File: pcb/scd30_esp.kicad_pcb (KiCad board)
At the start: 2 copper layers, 59.2 x 39.4 mm, 60 parts, among them J1 SCD30, J2 USB_C_Receptacle_USB2.0, J3 24P P0.5mm waveshare E-paper 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, J4 QWIIC, Q1 Si1308EDL, Q2 Q_NMOS_GSD, Q3 BSS138PS, Q4 Q_NMOS_GSD, SW1 SW_SPST, U1 TPS62A01PDDCR, U2 ESP32-WROOM-E, U3 CH340C, U4 TSOP38G36

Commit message: RC1
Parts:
- added D7: LED_Small, LED_SMD:LED_0603_1608Metric, B.Cu at (112.6, 79.7)
- added R17: 1k, Resistor_SMD:R_0603_1608Metric, B.Cu at (115.8, 79.7)
- moved R13 13.2 mm to (142.3, 80.8), turned to 180 degrees
- moved R12 11.7 mm to (145.3, 80.8), turned to 0 degrees
- moved Q2 3.22 mm to (156.4, 83.1), turned to 0 degrees
- moved R14 2.97 mm to (117.1, 105.6)
- moved Q4 2.97 mm to (117.0, 110.0)
- moved R15 2.97 mm to (117.1, 107.2)
- moved R11 2.94 mm to (160.7, 82.5)
- moved R16 2.73 mm to (117.0, 114.3), turned to 90 degrees
- moved C7 2.42 mm to (113.5, 109.2)
- moved C6 2.33 mm to (161.9, 85.4), turned to -90 degrees
- moved SW1 1.00 mm to (158.0, 114.7)
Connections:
- U2 pad 24: unconnected-(U2-ADC2_CH2/GPIO2-Pad24) -> /status_led
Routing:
- net +3V3: track 187.3 -> 204.3 mm
- net /status_led: track 0.00 -> 15.4 mm, vias 0 -> 1
- net Net-(Q2-G): track 2.08 -> 9.86 mm
- net Net-(D6-K): track 2.52 -> 8.22 mm
- net VBUS: track 46.4 -> 42.6 mm
- net /IR_TX_L: track 51.2 -> 48.0 mm
- net GND: track 102.8 -> 99.8 mm
- net Net-(D5-K): track 2.58 -> 5.56 mm
- net /QWIIC_SDA: track 61.0 -> 59.1 mm
- net /QWIIC_SCL: track 62.5 -> 60.8 mm
- net Net-(D7-A): track 0.00 -> 1.59 mm
- net /IR_TX_R: track 12.3 -> 10.8 mm
- net Net-(Q4-D): track 2.52 -> 1.91 mm
- net Net-(Q2-D): track 2.68 -> 2.15 mm

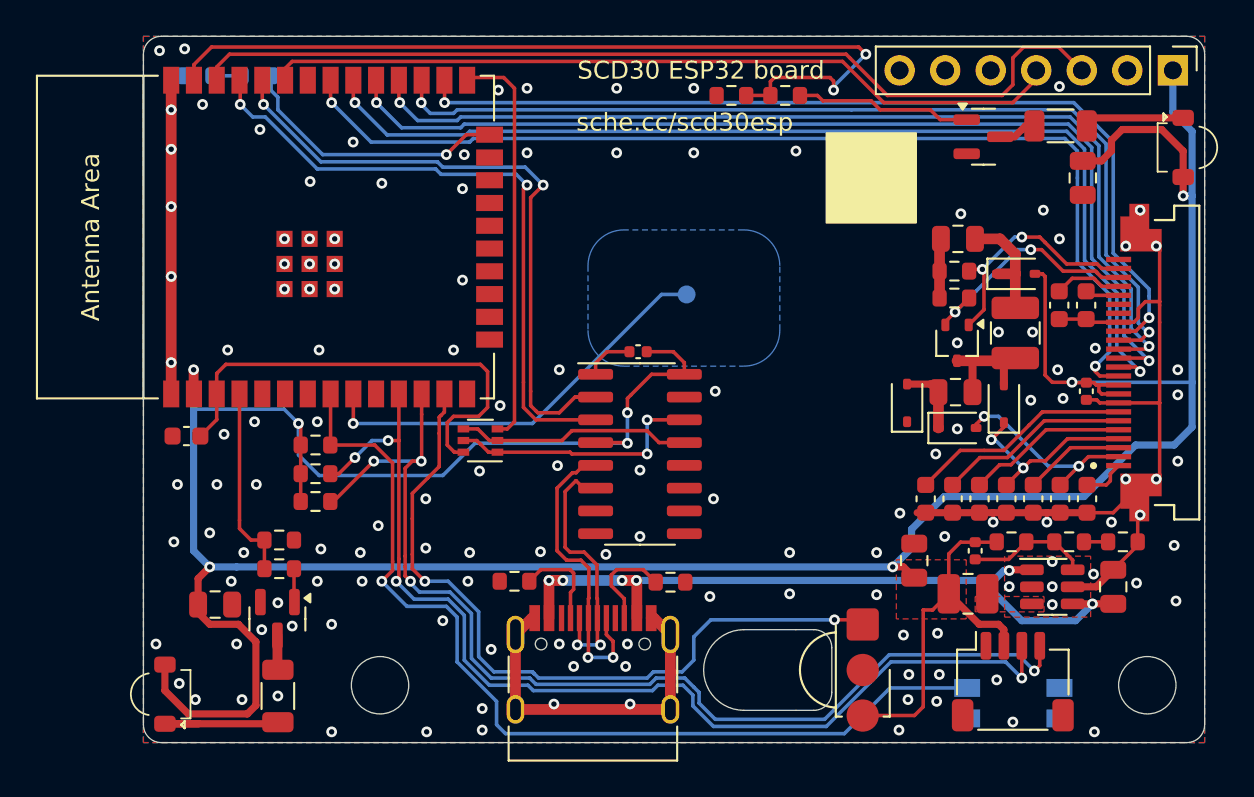
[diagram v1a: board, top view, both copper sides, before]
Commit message: Added alternate footprint for XFCN FPC connector
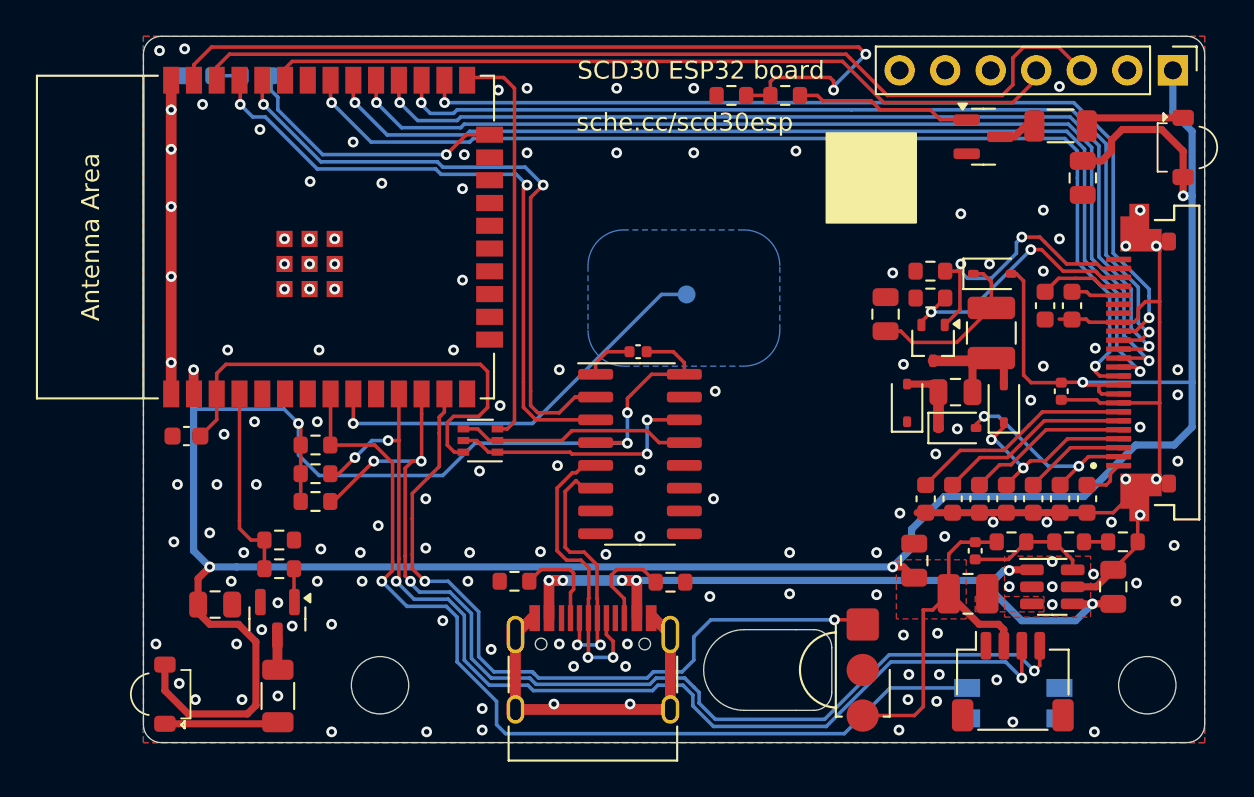
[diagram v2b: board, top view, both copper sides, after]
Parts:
- added REF**: XFCN_F0504-H-24-10G-R_1x24-1MP_P0.50mm_Horizontal, Connector_FFC-FPC:XFCN_F0504-H-24-10G-R_1x24-1MP_P0.50mm_Horizontal, F.Cu at (165.4, 95.7)
- moved C9 5.83 mm to (150.9, 93.0), turned to 90 degrees
- moved C20 1.40 mm to (160.7, 97.3)
- moved D1 1.34 mm to (156.8, 90.8)
- moved R6 1.34 mm to (153.4, 92.1)
- moved R7 1.34 mm to (153.4, 90.6)
- moved L2 1.34 mm to (156.8, 94.0)
- moved Q1 1.34 mm to (153.6, 94.6)
- moved C17 0.79 mm to (161.3, 92.5)
- moved C18 0.79 mm to (159.8, 92.5)
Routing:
- net Net-(D1-K): track 6.60 -> 9.61 mm
- net /Waveshare E-ink/GDR: track 13.3 -> 15.9 mm
- net GND: track 99.8 -> 97.9 mm, vias 136 -> 137
- net Net-(D6-K): track 8.22 -> 6.34 mm
- net /Waveshare E-ink/RESE: track 13.5 -> 14.4 mm
- net Net-(J3-Pin_21): track 3.80 -> 4.60 mm
- net /Waveshare E-ink/VSH2: track 1.91 -> 2.68 mm
- net +3V3: track 204.3 -> 205.0 mm

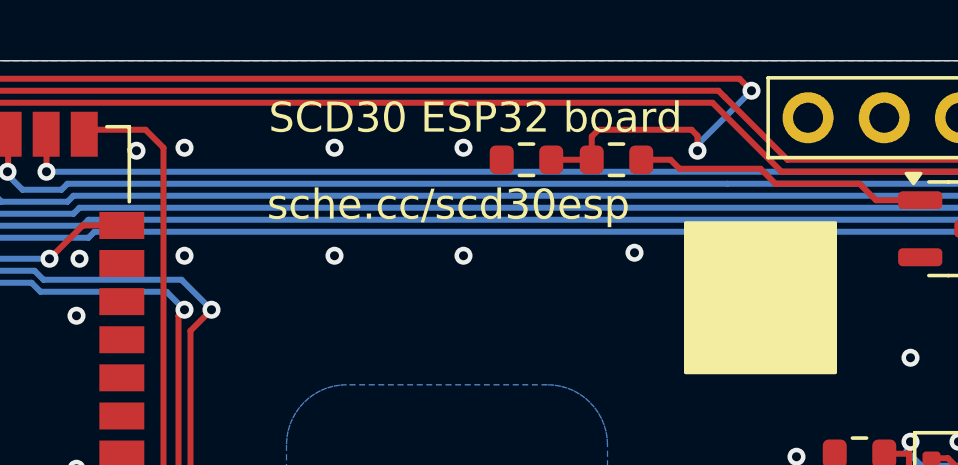
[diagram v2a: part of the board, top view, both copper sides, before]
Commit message: nudged components, added version text
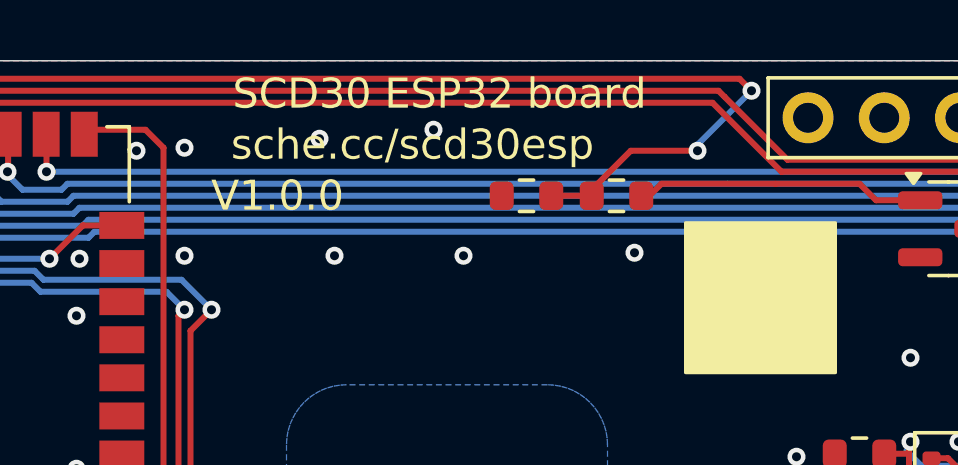
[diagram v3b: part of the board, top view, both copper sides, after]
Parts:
- moved R12 1.20 mm to (145.3, 82.0)
- moved R13 1.20 mm to (142.3, 82.0)
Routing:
- net /IR_TX_L: track 48.0 -> 47.1 mm
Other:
- board text added: "V1.0.0"
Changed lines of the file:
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@@
 	(footprint "Resistor_SMD:R_0603_1608Metric"
 		(layer "F.Cu")
-		(at 145.3 80.8)
+		(at 145.3 82)
 		(descr "Resistor SMD 0603 (1608 Metric), square (rectangular) end terminal, IPC_7351 nominal, (Body size source: IPC-SM-782 page 72, https://www.pcb-3d.com/wordpress/wp-content/uploads/ipc-sm-782a_amendment_1_and_2.pdf), generated with kicad-footprint-generator")
 		(tags "resistor")
@@
 	(footprint "Resistor_SMD:R_0603_1608Metric"
 		(layer "F.Cu")
-		(at 142.3 80.8 180)
+		(at 142.3 82 180)
 		(descr "Resistor SMD 0603 (1608 Metric), square (rectangular) end terminal, IPC_7351 nominal, (Body size source: IPC-SM-782 page 72, https://www.pcb-3d.com/wordpress/wp-content/uploads/ipc-sm-782a_amendment_1_and_2.pdf), generated with kicad-footprint-generator")
 		(tags "resistor")
@@
 		)
 	)
+	(gr_text "V1.0.0"
+		(at 112.6 115.8 -0)
+		(layer "B.SilkS")
+		(effects
+			(font
+				(size 1 1)
+				(thickness 0.15)
+			)
+			(justify mirror)
+		)
+	)
 	(gr_text "sche.cc/scd30esp"
-		(at 139.7 82.3 0)
+		(at 138.5 80.3 0)
 		(layer "F.SilkS")
 		(effects
@@
 	)
 	(gr_text "SCD30 ESP32 board"
-		(at 140.6 79.4 0)
+		(at 139.4 78.6 0)
+		(layer "F.SilkS")
+		(effects
+			(font
+				(size 1 1)
+				(thickness 0.15)
+			)
+		)
+	)
+	(gr_text "V1.0.0"
+		(at 134 82 0)
 		(layer "F.SilkS")
 		(effects
@@
 	)
 	(via
-		(at 140.2 80.4)
+		(at 139.2 79.8)
 		(size 0.6)
 		(drill 0.3)
@@
 	)
 	(via
-		(at 135.9 80.4)
+		(at 135.4 80.1)
 		(size 0.6)
 		(drill 0.3)
@@
 	)
 	(segment
-		(start 147.4 81.1)
-		(end 150.1 81.1)
-		(width 0.2)
-		(layer "F.Cu")
-		(net 67)
-	)
-	(segment
-		(start 147.1 80.8)
-		(end 147.4 81.1)
+		(start 150.6 81.6)
+		(end 153.4 81.6)
 		(width 0.2)
 		(layer "F.Cu")
@@
 	)
 	(segment
-		(start 150.6 81.6)
-		(end 153.4 81.6)
+		(start 146.4 82)
+		(end 146.8 81.6)
 		(width 0.2)
 		(layer "F.Cu")
@@
 	)
 	(segment
-		(start 146.125 80.8)
-		(end 147.1 80.8)
+		(start 153.95 82.15)
+		(end 155.425 82.15)
 		(width 0.2)
 		(layer "F.Cu")
@@
 	)
 	(segment
-		(start 153.95 82.15)
-		(end 155.425 82.15)
+		(start 146.125 82)
+		(end 146.4 82)
 		(width 0.2)
 		(layer "F.Cu")
@@
 	)
 	(segment
-		(start 150.1 81.1)
-		(end 150.6 81.6)
+		(start 150.6 81.6)
+		(end 146.8 81.6)
 		(width 0.2)
 		(layer "F.Cu")
@@
 	)
 	(segment
-		(start 144.475 80.025)
-		(end 144.475 80.8)
+		(start 144.475 82)
+		(end 143.125 82)
 		(width 0.2)
 		(layer "F.Cu")
@@
 	)
 	(segment
-		(start 149.4 78.1)
-		(end 149.8 78.5)
+		(start 148 80.5)
+		(end 145.775 80.5)
 		(width 0.2)
 		(layer "F.Cu")
@@
 	)
 	(segment
-		(start 147.8 79.8)
-		(end 144.7 79.8)
+		(start 149.4 78.1)
+		(end 149.8 78.5)
 		(width 0.2)
 		(layer "F.Cu")
@@
 	)
 	(segment
-		(start 148 80)
-		(end 147.8 79.8)
-		(width 0.2)
-		(layer "F.Cu")
-		(net 71)
-	)
-	(segment
 		(start 113.3 78.1)
 		(end 149.4 78.1)
@@
 	)
 	(segment
-		(start 144.7 79.8)
-		(end 144.475 80.025)
-		(width 0.2)
-		(layer "F.Cu")
-		(net 71)
-	)
-	(segment
-		(start 148 80.5)
-		(end 148 80)
+		(start 145.775 80.5)
+		(end 144.475 81.8)
 		(width 0.2)
 		(layer "F.Cu")
@@
 		(width 0.2)
 		(layer "F.Cu")
-		(net 71)
-	)
-	(segment
-		(start 144.475 80.8)
-		(end 143.125 80.8)
-		(width 0.2)
-		(layer "F.Cu")
